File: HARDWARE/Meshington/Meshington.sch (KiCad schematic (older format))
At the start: 22 parts

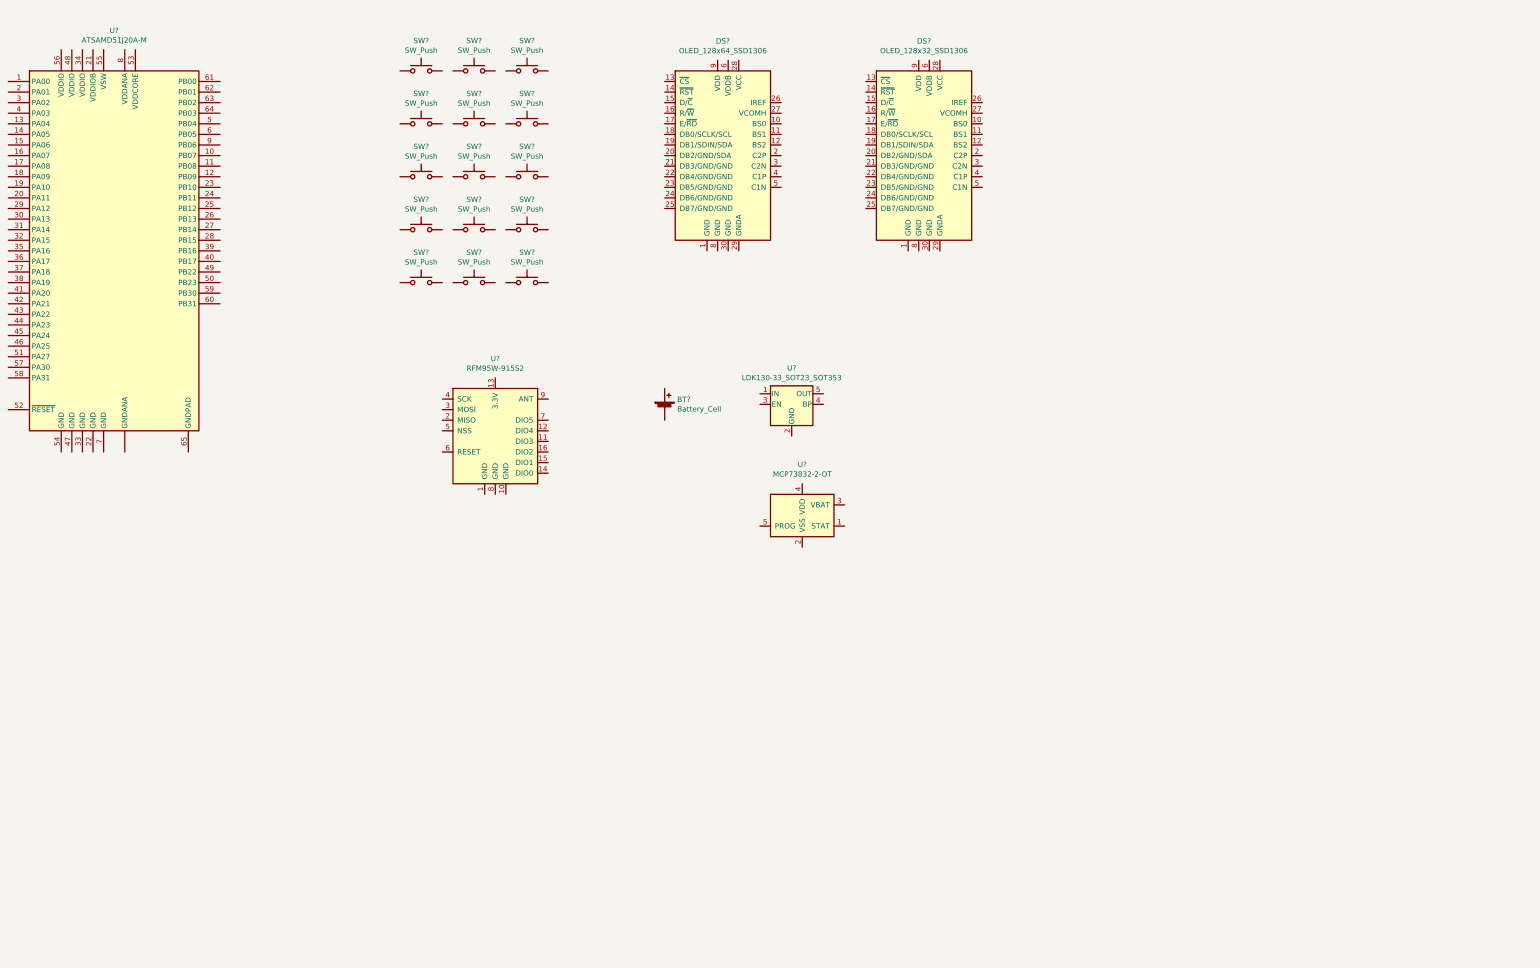
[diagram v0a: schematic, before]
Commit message: first pass schematic minus mcu
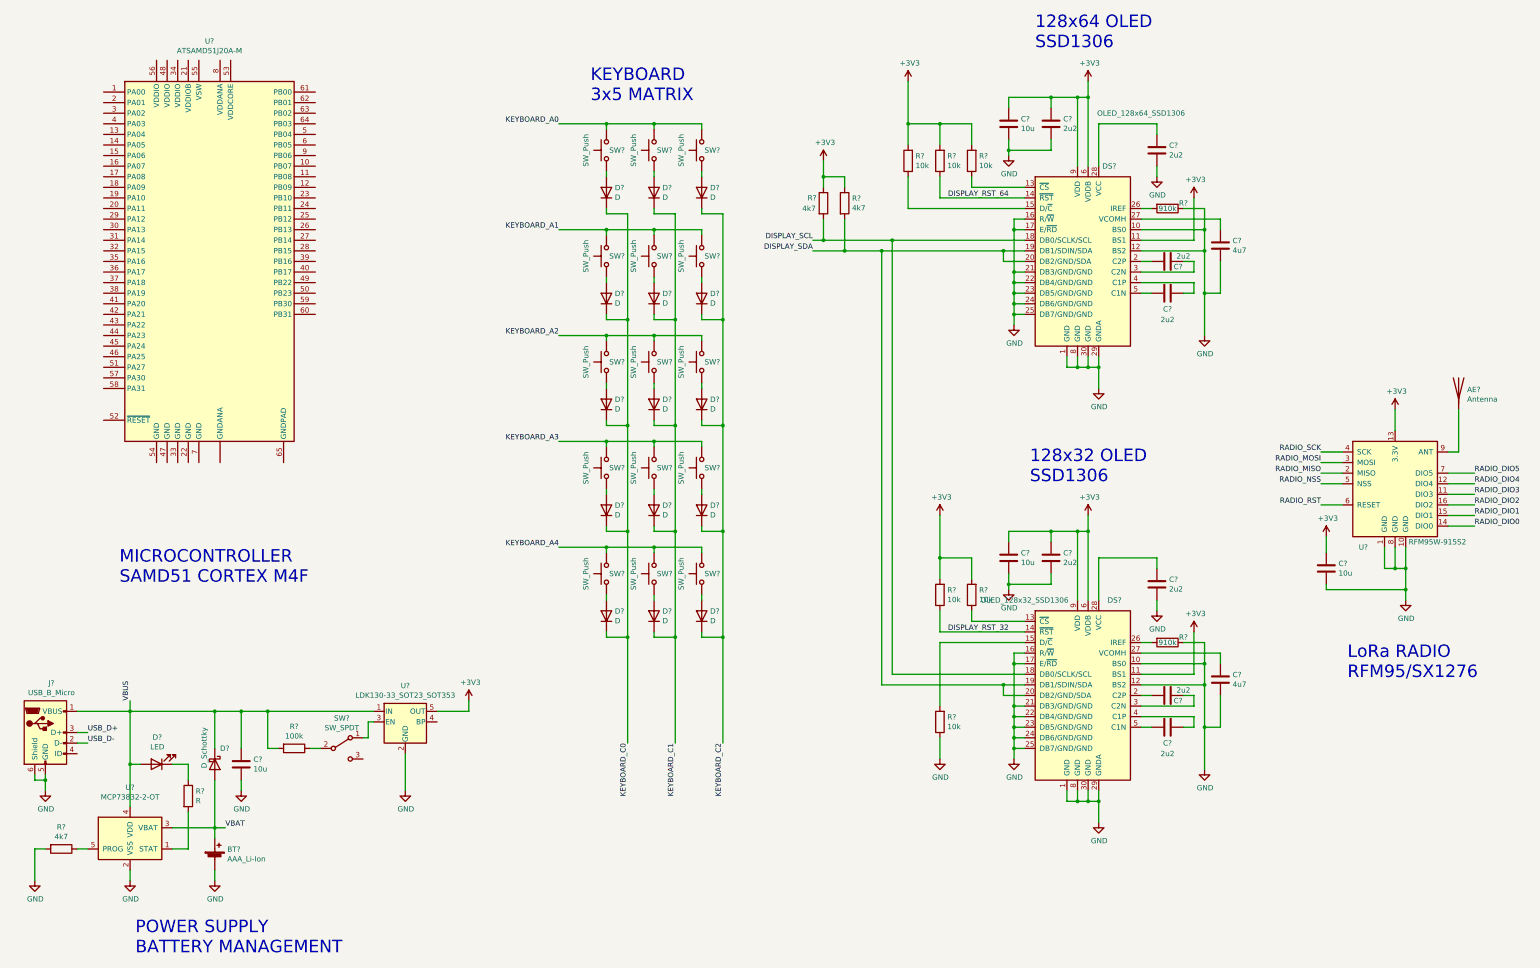
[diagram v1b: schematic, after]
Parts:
- removed SW? (x14): SW_Push, symbol Switch:SW_Push
- added AE?: Antenna, symbol Device:Antenna
- added C? (x4): 10u, symbol Device:C
- added C? (x8): 2u2, symbol Device:C
- added C? (x2): 4u7, symbol Device:C
- added D? (x15): D, symbol Device:D
- added D?: LED, symbol Device:LED
- added D?: D_Schottky, symbol Device:D_Schottky
- added J?: USB_B_Micro, symbol Connector:USB_B_Micro
- added R?: 100k, symbol Device:R
- added R?: R, symbol Device:R
- added R? (x3): 4k7, symbol Device:R
- added R? (x2): 910k, symbol Device:R
- added R? (x6): 10k, symbol Device:R
- added SW? (x14): SW_Push, symbol Switch:SW_Push
- added SW?: SW_SPDT, symbol Switch:SW_SPDT
- BT?: value Battery_Cell -> AAA_Li-Ion
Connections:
- net at SW?.1: now also D?.2 (A)
- net KEYBOARD_A0: now reaches SW?.2
- net KEYBOARD_A0: now also SW?.2, SW?.2
- net GND: now reaches DS?.1 (GND)
- net GND: now also BT?.2 (-), DS?.1 (GND), DS?.10 (BS0), DS?.10 (BS0), DS?.12 (BS2), DS?.12 (BS2), DS?.16 (R/~W~), DS?.16 (R/~W~), DS?.17 (E/~RD~), DS?.17 (E/~RD~), DS?.21 (DB3/GND/GND), DS?.21 (DB3/GND/GND), DS?.22 (DB4/GND/GND), DS?.22 (DB4/GND/GND), DS?.23 (DB5/GND/GND), DS?.23 (DB5/GND/GND), DS?.24 (DB6/GND/GND), DS?.24 (DB6/GND/GND), DS?.25 (DB7/GND/GND), DS?.25 (DB7/GND/GND), DS?.29 (GNDA), DS?.29 (GNDA), DS?.30 (GND), DS?.30 (GND), DS?.8 (GND), DS?.8 (GND), U?.1 (GND), U?.10 (GND), U?.2 (GND), U?.2 (VSS), U?.8 (GND), C?.2, C?.2, C?.2, C?.2, C?.2, C?.2, C?.2, C?.2, C?.2, C?.2, J?.5 (GND), J?.6 (Shield), R?.1, R?.1, R?.1, R?.2
- net +3V3: now reaches DS?.11 (BS1)
- net +3V3: now also DS?.11 (BS1), DS?.6 (VDDB), DS?.6 (VDDB), DS?.9 (VDD), DS?.9 (VDD), U?.13 (3.3V), U?.5 (OUT), C?.1, C?.1, C?.1, C?.1, C?.1, R?.1, R?.1, R?.2, R?.2, R?.2, R?.2, R?.2
- net at DS?.13 (~CS~): now also R?.1 (x2)
- net DISPLAY_RST_32: now reaches DS?.14 (~RST~)
- net DISPLAY_RST_32: now also R?.1
- net at DS?.15 (D/~C~): now also R?.2
- net DISPLAY_SCL: now reaches DS?.18 (DB0/SCLK/SCL)
- net DISPLAY_SCL: now also DS?.18 (DB0/SCLK/SCL), R?.2
- net DISPLAY_SDA: now reaches DS?.19 (DB1/SDIN/SDA)
- net DISPLAY_SDA: now also DS?.19 (DB1/SDIN/SDA), DS?.20 (DB2/GND/SDA), DS?.20 (DB2/GND/SDA), R?.2
- net at DS?.2 (C2P): now also C?.2 (x2)
- net at DS?.26 (IREF): now also R?.2 (x2)
- net at DS?.27 (VCOMH): now also C?.1 (x2)
- net at DS?.28 (VCC): now also C?.1 (x2)
- net at DS?.3 (C2N): now also C?.1 (x2)
- net at DS?.4 (C1P): now also C?.1 (x2)
- net at DS?.5 (C1N): now also C?.2 (x2)
- net DISPLAY_RST_64: now reaches DS?.14 (~RST~)
- net DISPLAY_RST_64: now also R?.1
- net at DS?.15 (D/~C~): now also R?.1
- net RADIO_DIO3: now reaches U?.11 (DIO3)
- net RADIO_DIO4: now reaches U?.12 (DIO4)
- net RADIO_DIO0: now reaches U?.14 (DIO0)
- net RADIO_DIO1: now reaches U?.15 (DIO1)
- net RADIO_DIO2: now reaches U?.16 (DIO2)
- net RADIO_MISO: now reaches U?.2 (MISO)
- net RADIO_MOSI: now reaches U?.3 (MOSI)
- net RADIO_SCK: now reaches U?.4 (SCK)
- net RADIO_NSS: now reaches U?.5 (NSS)
- net RADIO_RST: now reaches U?.6 (RESET)
- net RADIO_DIO5: now reaches U?.7 (DIO5)
- net at U?.9 (ANT): now also AE?.1 (A)
- net VBAT: now reaches BT?.1 (+)
- net VBAT: now also U?.3 (VBAT), D?.2 (A)
- net VBUS: now reaches U?.1 (IN)
- net VBUS: now also U?.4 (VDD), C?.1, D?.1 (K), D?.2 (A), J?.1 (VBUS), R?.2
- net at U?.3 (EN): now also SW?.1 (A)
- net at U?.1 (STAT): now also R?.2
- net at U?.5 (PROG): now also R?.1
- new net: D?.2 (A), SW?.1 (x14)
- new net: R?.1, SW?.2 (B)
- new net: D?.1 (K), R?.1
- new net KEYBOARD_A1: SW?.2, SW?.2, SW?.2
- new net KEYBOARD_A2: SW?.2, SW?.2, SW?.2
- new net KEYBOARD_A3: SW?.2, SW?.2, SW?.2
- new net KEYBOARD_A4: SW?.2, SW?.2, SW?.2
- new net KEYBOARD_C0: D?.1 (K), D?.1 (K), D?.1 (K), D?.1 (K), D?.1 (K)
- new net KEYBOARD_C1: D?.1 (K), D?.1 (K), D?.1 (K), D?.1 (K), D?.1 (K)
- new net KEYBOARD_C2: D?.1 (K), D?.1 (K), D?.1 (K), D?.1 (K), D?.1 (K)
- new net USB_D+: J?.3 (D+)
- new net USB_D-: J?.2 (D-)
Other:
- note added: "128x32 OLED\nSSD1306"
- note added: "128x64 OLED\nSSD1306"
- note added: "KEYBOARD\n3x5 MATRIX"
- note added: "LoRa RADIO\nRFM95/SX1276"
- note added: "MICROCONTROLLER\nSAMD51 CORTEX M4F"
- note added: "POWER SUPPLY\nBATTERY MANAGEMENT"
- moved on the sheet: BT?, DS?, SW?, U?
